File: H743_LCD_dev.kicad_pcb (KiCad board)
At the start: 6 copper layers, 76 x 78 mm, 114 parts, among them J1 Micro_SD_Card_Det_Hirose_DM3AT, J2 TFT_LCD, J3 swd, J4 USB-C, J5 I2C-STEMMA-QT, J6 UART, J8 SPKR, J9 UART, SW1 SW_Push, SW2 SW_Push, SW3 SW_Push, SW4 SW_Push, U1 W25Q128JVS, U2 IS42S16160J-7TL, U3 MT9284, U4 STM32H723ZGTx, U5 W25N01GVZEIG, U6 MAX98357AETE_, U7 CAT24C128, U8 TLV75733PDBV, Y1 25MHz, Y2 32.768KHz

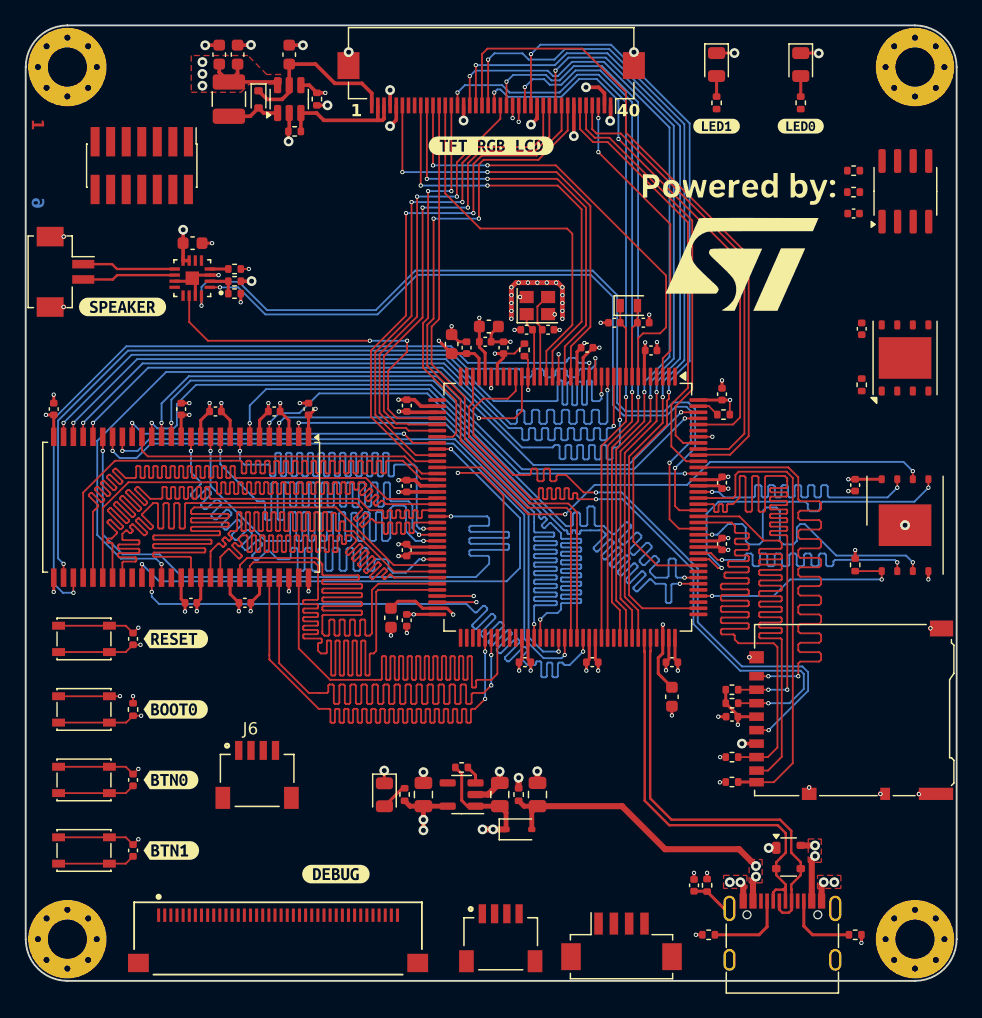
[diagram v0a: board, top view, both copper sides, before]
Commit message: Changed the FPC footprint and uart, added RTC battery connector
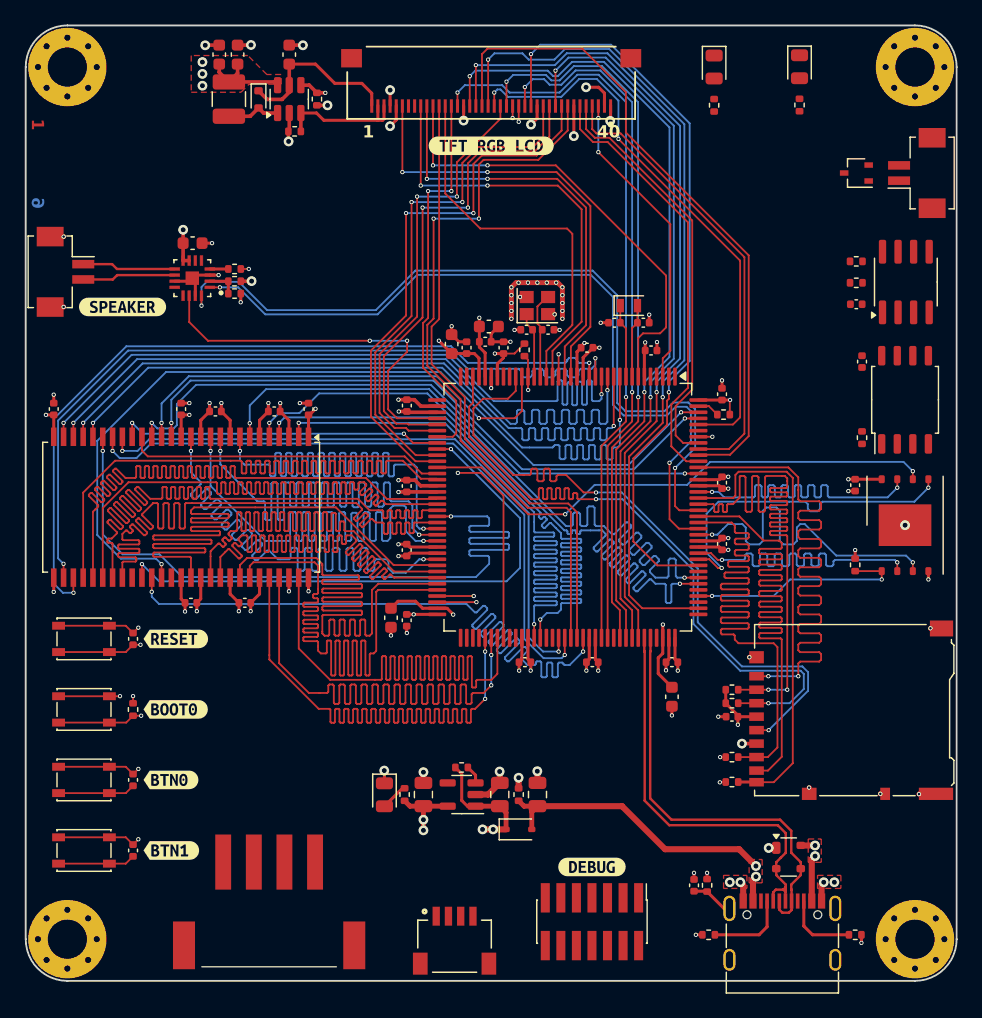
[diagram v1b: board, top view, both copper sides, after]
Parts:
- removed the G*** at (164.4, 67.8)
- removed J7: ~, FPC-40P-Omron-XF2M-4015-1Apretty:Omron-XF2M-4015-1A-R100-0-0-0
- removed U5: W25N01GVZEIG, Package_SON:WSON-8-1EP_6x5mm_P1.27mm_EP3.4x4.3mm
- removed kibuzzard-6641818D: G***, kibuzzard-6641818D
- removed kibuzzard-66418194: G***, kibuzzard-66418194
- added D7: BAT54CW, Package_TO_SOT_SMD:SOT-323_SC-70, F.Cu at (174.0, 60.4)
- added U9: W25Q128JVS, Package_SO:SOIC-8_5.23x5.23mm_P1.27mm, F.Cu at (178.0, 78.9)
- J2: footprint Connector_FFC-FPC:Hirose_FH12-40S-0.5SH_1x40-1MP_P0.50mm_Horizontal -> FPC-40P-Omron-XF2M-4015-1Apretty:Omron-XF2M-4015-1A-R100-0-0-0
- J6: value UART -> BAT; footprint SM04B-SRSS-TB_LF__SN_:JST_SM04B-SRSS-TB_LF__SN_ -> Connector_Hirose:Hirose_DF13C_CL535-0402-2-51_1x02-1MP_P1.25mm_Vertical
- J9: footprint Connector_Hirose:Hirose_DF13C_CL535-0404-8-51_1x04-1MP_P1.25mm_Vertical -> S4B-XH-SM4-TB_LF__SN:S4BXHSM4TBLFSN
- U1: value W25Q128JVS -> MT25Q
- moved J3 71.8 mm to (152.4, 121.5)
- moved J6 71.6 mm to (178.9, 60.4), turned to 90 degrees
- moved J9 28.9 mm to (126.1, 120.9)
- moved kibuzzard-66417165 20.9 mm to (152.4, 117.0)
- moved C20 7.41 mm to (174.0, 71.1)
- moved R5 7.41 mm to (174.0, 69.4)
- moved R6 7.41 mm to (174.0, 67.6)
- moved U7 7.41 mm to (178.1, 69.3)
- moved R1 4.32 mm to (174.5, 82.0)
- moved J5 3.77 mm to (141.2, 121.1)
- moved C22 2.68 mm to (174.5, 75.8)
- moved D6 0.28 mm to (162.4, 51.7)
- moved R24 0.28 mm to (162.4, 54.9)
- moved D5 0.20 mm to (169.4, 51.7)
- moved R23 0.20 mm to (169.4, 54.8)
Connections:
- J6 pad 1: unconnected-(J6-Pad1) -> VBAT
- J6 pad 2: unconnected-(J6-Pad2) -> GND
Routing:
- net GND: track 136.2 -> 131.0 mm, vias 95 -> 91
- net Net-(D6-A): track 1.68 -> 0.00 mm
- net Net-(D5-A): track 1.68 -> 0.00 mm

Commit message: Added UART esd
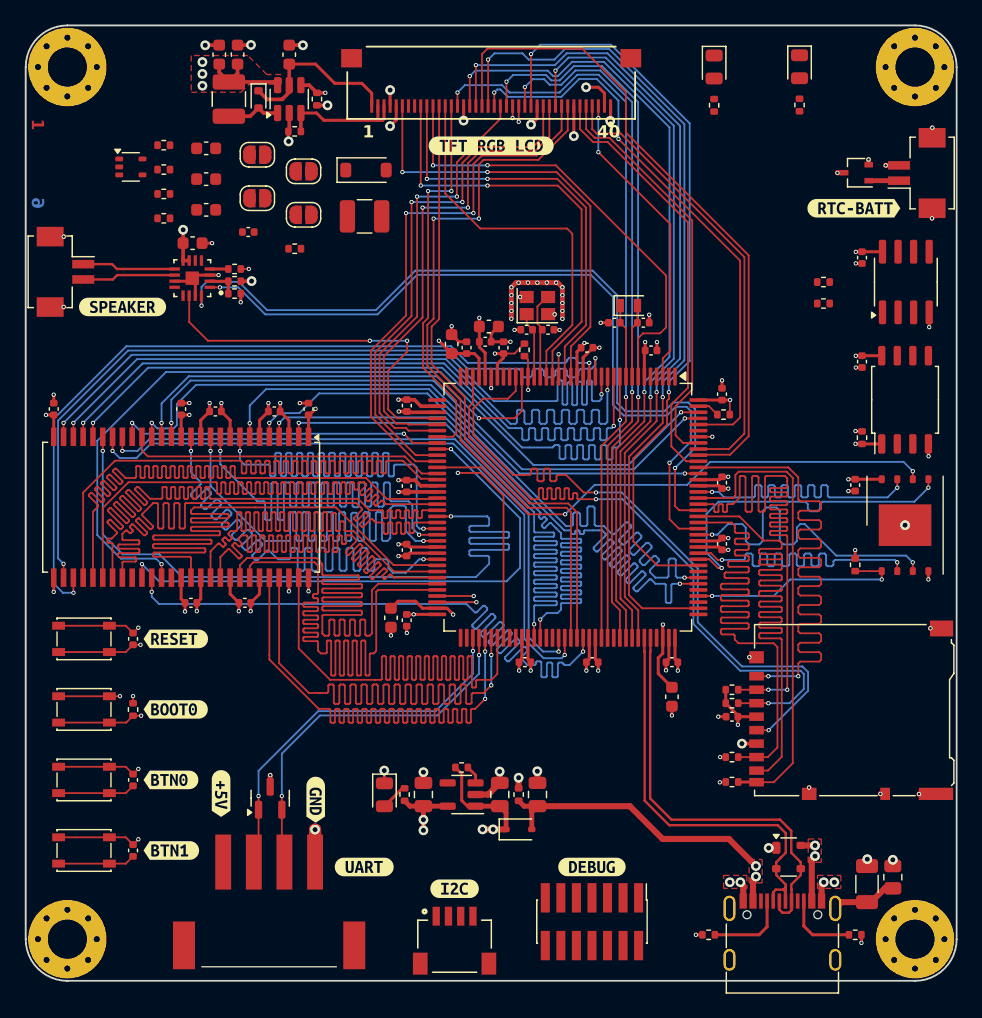
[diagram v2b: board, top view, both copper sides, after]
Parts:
- added C46: 1u, Capacitor_SMD:C_0603_1608Metric, F.Cu at (120.9, 58.4)
- added C47: 1u, Capacitor_SMD:C_0603_1608Metric, F.Cu at (120.9, 60.9)
- added C48: 10u, Capacitor_SMD:C_0603_1608Metric, F.Cu at (120.9, 63.4)
- added C49: 100n, Capacitor_SMD:C_0402_1005Metric, F.Cu at (124.4, 65.2)
- added D8: MBR0540, Diode_SMD:D_SOD-123, F.Cu at (134.0, 60.2)
- added D9: ESDA14V2L, Package_TO_SOT_SMD:SOT-23, F.Cu at (126.2, 111.4)
- added JP1: JMP, Jumper:SolderJumper-2_P1.3mm_Open_RoundedPad1.0x1.5mm, F.Cu at (125.1, 58.9)
- added JP2: JMP, Jumper:SolderJumper-2_P1.3mm_Open_RoundedPad1.0x1.5mm, F.Cu at (125.1, 62.4)
- added JP3: JMP, Jumper:SolderJumper-2_P1.3mm_Open_RoundedPad1.0x1.5mm, F.Cu at (128.9, 60.3)
- added JP4: JMP, Jumper:SolderJumper-2_P1.3mm_Open_RoundedPad1.0x1.5mm, F.Cu at (128.9, 63.8)
- added L2: 6.8u, Inductor_SMD:L_1210_3225Metric, F.Cu at (133.9, 63.9)
- added R25: 8.2R, Resistor_SMD:R_0402_1005Metric, F.Cu at (117.5, 58.1)
- added R26: 8.2R, Resistor_SMD:R_0402_1005Metric, F.Cu at (117.5, 60.1)
- added R27: 4.3R, Resistor_SMD:R_0402_1005Metric, F.Cu at (117.5, 62.1)
- added R28: 2.0R, Resistor_SMD:R_0402_1005Metric, F.Cu at (117.5, 64.1)
- added R29: 10K, Resistor_SMD:R_0402_1005Metric, F.Cu at (128.2, 66.6)
- added U5: TPS61169, Package_TO_SOT_SMD:SOT-353_SC-70-5, F.Cu at (114.8, 59.9)
- added kibuzzard-6642BE54: G***, kibuzzard-6642BE54, F.Cu at (133.8, 117.0)
- added kibuzzard-6642BE6C: G***, kibuzzard-6642BE6C, F.Cu at (141.2, 118.8)
- added kibuzzard-6642BE85: G***, kibuzzard-6642BE85, F.Cu at (173.8, 63.3)
- added kibuzzard-664329E8: G***, kibuzzard-664329E8, F.Cu at (122.1, 111.0)
- added kibuzzard-664329F6: G***, kibuzzard-664329F6, F.Cu at (129.9, 111.6)
- C30: value 1u -> 1uF/0805
- C43: value 4n7 -> 1nF/500V; footprint Capacitor_SMD:C_0402_1005Metric -> Capacitor_SMD:C_1206_3216Metric
- C45: value 10u -> 10uF/0805
- R13: value 1M -> 1M/0805; footprint Resistor_SMD:R_0402_1005Metric -> Resistor_SMD:R_0805_2012Metric
- moved R13 15.2 mm to (177.0, 117.9)
- moved C43 14.1 mm to (174.9, 118.4)
- moved C20 3.84 mm to (174.5, 67.3), turned to -90 degrees
- moved R5 3.17 mm to (171.3, 71.0)
- moved R6 3.17 mm to (171.3, 69.3)
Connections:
- C11 pad 1: +3V3 -> VBAT
- D7 pad 1: unconnected-(D7-Pad1) -> VB
- D7 pad 2: unconnected-(D7-Pad2) -> +3V3
- D7 pad 3: unconnected-(D7-Pad3) -> VBAT
- J6 pad 1: VBAT -> VB
- J9 pad 1: unconnected-(J9-Pin_1-Pad1) -> +5V
- J9 pad 2: unconnected-(J9-Pin_2-Pad2) -> /IO/USART_RX
- J9 pad 3: unconnected-(J9-Pin_3-Pad3) -> /IO/USART_TX
- J9 pad 4: unconnected-(J9-Pin_4-Pad4) -> GND
- U4 pad 6: +3V3 -> VBAT
- U4 pad 75: /MCU/PB14 -> /IO/USART_RX
- U4 pad 76: /MCU/PB15 -> /IO/USART_TX
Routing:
- net /IO/USART_RX: track 0.00 -> 31.3 mm, vias 0 -> 2
- net /IO/USART_TX: track 0.00 -> 30.7 mm, vias 0 -> 2
- net VBAT: track 0.00 -> 30.0 mm, vias 0 -> 2
- net GND: track 131.0 -> 140.7 mm, vias 91 -> 100
- net VB: track 0.00 -> 2.48 mm
- net +3V3: track 94.2 -> 96.7 mm, vias 32 -> 35
- net /MEMORY/~{NAND_CS}: track 0.00 -> 2.14 mm, vias 0 -> 1
- net Net-(J4-SHIELD): track 3.47 -> 5.37 mm

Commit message: All clear (need to verify). LCD backlight driver left untracked
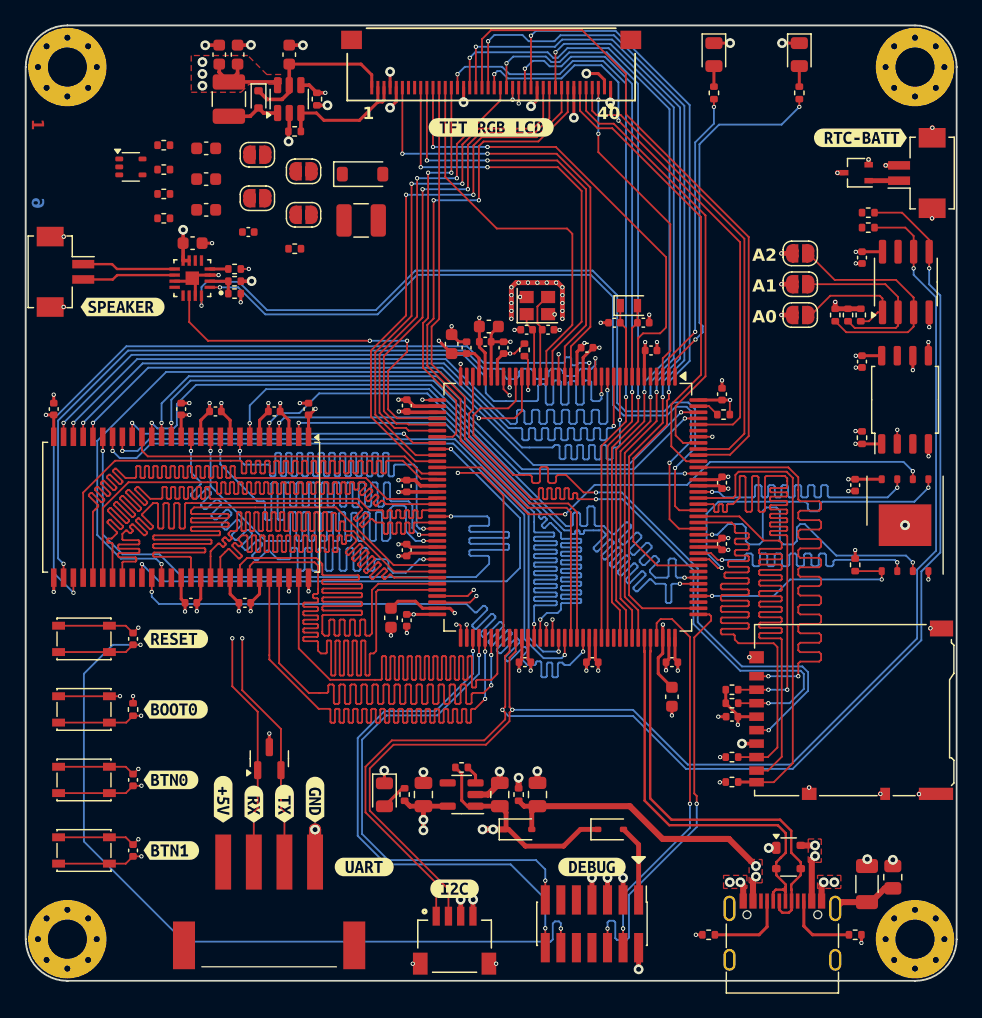
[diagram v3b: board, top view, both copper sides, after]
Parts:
- removed J3: swd, Connector_PinHeader_1.27mm:PinHeader_2x07_P1.27mm_Vertical_SMD
- removed kibuzzard-66418113: G***, kibuzzard-66418113
- added D10: NSR0320MW2T1G, Diode_SMD:D_SOD-323, F.Cu at (153.9, 114.0)
- added J7: swd, Connector_PinHeader_1.27mm:PinHeader_2x07_P1.27mm_Vertical_SMD, F.Cu at (152.4, 121.7)
- added JP5: JMP, Jumper:SolderJumper-2_P1.3mm_Open_RoundedPad1.0x1.5mm, F.Cu at (169.4, 67.0)
- added JP6: JMP, Jumper:SolderJumper-2_P1.3mm_Open_RoundedPad1.0x1.5mm, F.Cu at (169.4, 69.5)
- added JP7: JMP, Jumper:SolderJumper-2_P1.3mm_Open_RoundedPad1.0x1.5mm, F.Cu at (169.4, 72.0)
- added R30: 10K, Resistor_SMD:R_0402_1005Metric, F.Cu at (174.4, 72.0)
- added R31: 10K, Resistor_SMD:R_0402_1005Metric, F.Cu at (173.3, 72.0)
- added R32: 10K, Resistor_SMD:R_0402_1005Metric, F.Cu at (172.3, 72.0)
- added kibuzzard-6644A0DC: G***, kibuzzard-6644A0DC, F.Cu at (114.1, 71.3)
- added kibuzzard-6644A120: G***, kibuzzard-6644A120, F.Cu at (124.8, 111.9)
- added kibuzzard-6644A126: G***, kibuzzard-6644A126, F.Cu at (127.3, 111.9)
- moved R5 8.27 mm to (175.0, 63.6), turned to 0 degrees
- moved kibuzzard-6642BE85 5.77 mm to (174.3, 57.5)
- moved R6 5.76 mm to (175.0, 64.8), turned to 0 degrees
- moved D9 3.23 mm to (126.1, 108.2)
- moved J2 1.50 mm to (144.2, 51.5)
- moved kibuzzard-66417197 1.50 mm to (144.2, 56.7)
- moved D6 1.01 mm to (162.4, 50.7)
- moved R24 1.01 mm to (162.4, 53.8)
- moved D5 0.99 mm to (169.4, 50.7)
- moved R23 0.99 mm to (169.4, 53.8)
- moved kibuzzard-664329E8 0.50 mm to (122.3, 111.5)
- moved D8 0.43 mm to (133.7, 60.5)
- moved L2 0.43 mm to (133.6, 64.3)
- moved kibuzzard-664329F6 0.05 mm to (129.8, 111.6)
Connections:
- net /MCU/NRST renamed /IO/NRST
- D9 pad 1: /IO/USART_RX -> /IO/USART2_RX
- D9 pad 2: /IO/USART_TX -> /IO/USART2_TX
- J5 pad 1: unconnected-(J5-Pad1) -> /IO/STEMMA_SCL
- J5 pad 2: unconnected-(J5-Pad2) -> /IO/STEMMA_SDA
- J5 pad 3: unconnected-(J5-Pad3) -> +3V3
- J5 pad 4: unconnected-(J5-Pad4) -> GND
- J5 pad S1: Net-(J5-SHIELD-PadS1) -> GND
- J5 pad S2: Net-(J5-SHIELD-PadS1) -> GND
- J9 pad 2: /IO/USART_RX -> /IO/USART2_RX
- J9 pad 3: /IO/USART_TX -> /IO/USART2_TX
- R1 pad 2: /MEMORY/~{NAND_CS} -> /MCU/~{SPI_CS}
- R5 pad 2: /MEMORY/SDA -> /IO/STEMMA_SCL
- R6 pad 2: /MEMORY/SCL -> /IO/STEMMA_SDA
- U4 pad 1: /MCU/PE2 -> /MCU/LED_0
- U4 pad 105: /MCU/PA13(JTMS -> /IO/SWDIO
- U4 pad 109: /MCU/PA14(JTCK -> /IO/SWCLK
- U4 pad 2: /MCU/PE3 -> /MCU/LED_1
- U4 pad 28: /MCU/PC2_C -> /MCU/SPI_MISO
- U4 pad 29: /MCU/PC3_C -> /MCU/SPI_MOSI
- U4 pad 36: /MCU/PA2 -> /IO/USART2_TX
- U4 pad 37: /MCU/PA3 -> /IO/USART2_RX
- U4 pad 73: /MCU/PB12 -> /MCU/~{SPI_CS}
- U4 pad 74: /MCU/PB13 -> /MCU/SPI_CLK
- U4 pad 75: /IO/USART_RX -> /IO/USART1_TX
- U4 pad 76: /IO/USART_TX -> /IO/USART1_RX
- U4 pad 81: /MCU/PD12 -> /IO/STEMMA_SCL
- U4 pad 82: /MCU/PD13 -> /IO/STEMMA_SDA
- U4 pad 87: /MCU/PG2 -> /MCU/BTN0
- U4 pad 88: /MCU/PG3 -> /MCU/BTN1
- U7 pad 1: GND -> Net-(JP7-A)
- U7 pad 2: GND -> Net-(JP6-A)
- U7 pad 3: GND -> Net-(JP5-A)
- U7 pad 5: /MEMORY/SDA -> /IO/STEMMA_SCL
- U7 pad 6: /MEMORY/SCL -> /IO/STEMMA_SDA
- U9 pad 1: /MEMORY/~{NAND_CS} -> /MCU/~{SPI_CS}
- U9 pad 2: /MEMORY/NAND_DO(IO1) -> /MCU/SPI_MISO
- U9 pad 3: /MEMORY/NAND_IO2 -> unconnected-(U9-IO2-Pad3)
- U9 pad 5: /MEMORY/NAND_DI(IO0) -> /MCU/SPI_MOSI
- U9 pad 6: /MEMORY/NAND_CLK -> /MCU/SPI_CLK
- U9 pad 7: /MEMORY/NAND_IO3 -> unconnected-(U9-IO3-Pad7)
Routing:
- net /IO/STEMMA_SCL: track 0.00 -> 114.3 mm, vias 0 -> 2
- net /IO/STEMMA_SDA: track 0.00 -> 111.8 mm, vias 0 -> 2
- net /IO/NRST: track 59.3 -> 123.4 mm, vias 2 -> 3
- net /IO/USART2_TX: track 0.00 -> 62.3 mm, vias 0 -> 2
- net /IO/USART2_RX: track 0.00 -> 60.4 mm, vias 0 -> 2
- net /MCU/SPI_CLK: track 0.00 -> 58.3 mm, vias 0 -> 2
- net /MCU/~{SPI_CS}: track 0.00 -> 51.0 mm, vias 0 -> 2
- net /MCU/BTN1: track 6.33 -> 54.6 mm, vias 0 -> 2
- net /IO/USART1_TX: track 0.00 -> 43.9 mm, vias 0 -> 2
- net /MCU/BTN0: track 6.33 -> 49.0 mm, vias 0 -> 2
- net /MCU/SPI_MOSI: track 0.00 -> 41.8 mm, vias 0 -> 2
- net /IO/USART1_RX: track 0.00 -> 41.1 mm, vias 0 -> 2
- net /MCU/SPI_MISO: track 0.00 -> 38.0 mm, vias 0 -> 2
- net /IO/SWCLK: track 0.00 -> 35.6 mm, vias 0 -> 2
- net /IO/SWDIO: track 0.00 -> 32.3 mm, vias 0 -> 2
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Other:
- board text added: "A0"
- board text added: "A1"
- board text added: "A2"

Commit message: All clear (need verification), need add capacitor next to I2C conn, verify I2S gain
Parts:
- removed C31: 1u, Capacitor_SMD:C_0603_1608Metric
- removed C32, C33: 10u, Capacitor_SMD:C_0603_1608Metric
- removed D1: MSK4010, Diode_SMD:D_SOD-523
- removed L1: 10uH, Inductor_SMD:L_1210_3225Metric
- removed R3: 2.74R, Resistor_SMD:R_0402_1005Metric
- removed R4: 5K1, Resistor_SMD:R_0402_1005Metric
- removed U3: MT9284, Package_TO_SOT_SMD:SOT-23-6
- moved L2 14.2 mm to (125.0, 53.0), turned to 180 degrees
- moved D8 13.5 mm to (125.0, 50.2), turned to 180 degrees
- moved JP3 13.2 mm to (116.2, 56.6)
- moved C47 12.6 mm to (128.8, 50.9), turned to 90 degrees
- moved C46 12.0 mm to (130.4, 50.9), turned to 90 degrees
- moved U5 10.9 mm to (125.0, 56.0)
- moved C48 10.9 mm to (128.3, 55.4)
- moved R28 10.2 mm to (119.5, 54.1), turned to 180 degrees
- moved R29 9.91 mm to (128.3, 56.7), turned to 180 degrees
- moved JP1 9.89 mm to (116.2, 63.1)
- moved JP2 9.32 mm to (116.2, 59.9)
- moved C49 9.19 mm to (122.6, 56.2), turned to 90 degrees
- moved JP4 7.56 mm to (131.4, 56.7), turned to 180 degrees
- moved R27 7.00 mm to (119.5, 55.4), turned to 180 degrees
- moved R25 4.35 mm to (121.4, 56.2), turned to 90 degrees
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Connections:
- net Net-(J4-SHIELD) renamed /MCU/SHIELD
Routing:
- net /LCD/LED_K: track 11.5 -> 24.8 mm
- net Net-(JP1-B): track 0.00 -> 7.34 mm
- net Net-(JP4-B): track 0.00 -> 5.54 mm
- net Net-(D8-A): track 0.00 -> 5.49 mm
- net Net-(JP2-B): track 0.00 -> 5.36 mm
- net Net-(D1-A): track 4.43 -> 0.00 mm
- net GND: track 156.0 -> 159.6 mm, vias 108 -> 110
- net /LCD/LED_A: track 13.4 -> 9.90 mm
- net VDD: track 30.4 -> 26.9 mm, vias 7 -> 6
- net Net-(JP3-B): track 0.00 -> 3.39 mm
- net /LCD/LCD_BLK: track 44.6 -> 42.9 mm
- net +3V3: track 101.4 -> 103.0 mm, vias 40 -> 43
- added copper zone on F.Cu, net /MCU/SHIELD
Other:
- board text added: "100mA"
- board text added: "25mA"
- board text added: "50mA"
- board text added: "Backlight current"
